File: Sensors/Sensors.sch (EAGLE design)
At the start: 32 parts, among them J2 JST_CONNECTOR, J6 JST_CONNECTOR, J7 JST_CONNECTOR, J8 JST_CONNECTOR, J9 JST_CONNECTOR

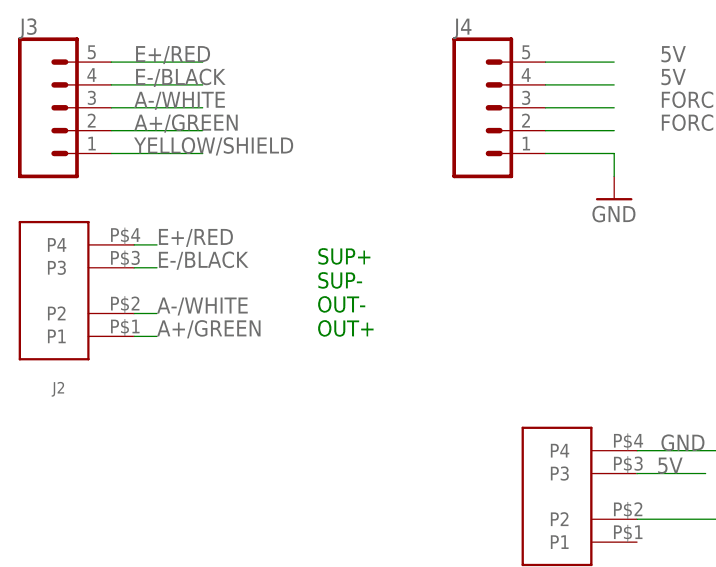
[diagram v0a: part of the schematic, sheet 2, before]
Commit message: Rewired force JST mount
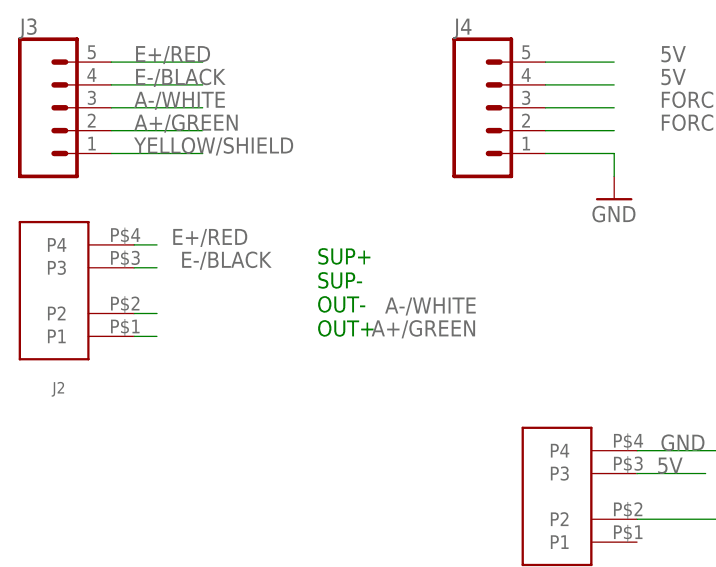
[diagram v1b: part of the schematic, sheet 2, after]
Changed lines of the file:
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@@
 <pinref part="J2" gate="G$1" pin="P4"/>
 <wire x1="2.54" y1="99.06" x2="5.08" y2="99.06" width="0.1524" layer="91"/>
-<label x="5.08" y="99.06" size="1.778" layer="95"/>
+<label x="15.24" y="99.06" size="1.778" layer="95" align="bottom-right"/>
 </segment>
 </net>
@@
 <pinref part="J2" gate="G$1" pin="P3"/>
 <wire x1="2.54" y1="96.52" x2="5.08" y2="96.52" width="0.1524" layer="91"/>
-<label x="5.08" y="96.52" size="1.778" layer="95"/>
+<label x="17.78" y="96.52" size="1.778" layer="95" align="bottom-right"/>
 </segment>
 </net>
@@
 <pinref part="J2" gate="G$1" pin="P2"/>
 <wire x1="2.54" y1="91.44" x2="5.08" y2="91.44" width="0.1524" layer="91"/>
-<label x="5.08" y="91.44" size="1.778" layer="95"/>
+<label x="40.64" y="91.44" size="1.778" layer="95" align="bottom-right"/>
 </segment>
 </net>
@@
 <pinref part="J2" gate="G$1" pin="P1"/>
 <wire x1="2.54" y1="88.9" x2="5.08" y2="88.9" width="0.1524" layer="91"/>
-<label x="5.08" y="88.9" size="1.778" layer="95"/>
+<label x="40.64" y="88.9" size="1.778" layer="95" align="bottom-right"/>
 </segment>
 </net>

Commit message: Refixed names on load cell JST
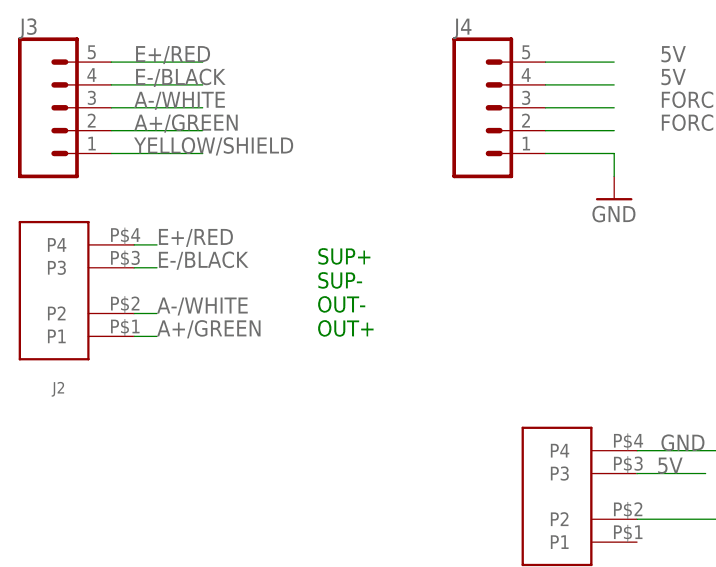
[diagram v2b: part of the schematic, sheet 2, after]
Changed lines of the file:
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@@
 <pinref part="J2" gate="G$1" pin="P4"/>
 <wire x1="2.54" y1="99.06" x2="5.08" y2="99.06" width="0.1524" layer="91"/>
-<label x="15.24" y="99.06" size="1.778" layer="95" align="bottom-right"/>
+<label x="5.08" y="99.06" size="1.778" layer="95"/>
 </segment>
 </net>
@@
 <pinref part="J2" gate="G$1" pin="P3"/>
 <wire x1="2.54" y1="96.52" x2="5.08" y2="96.52" width="0.1524" layer="91"/>
-<label x="17.78" y="96.52" size="1.778" layer="95" align="bottom-right"/>
+<label x="5.08" y="96.52" size="1.778" layer="95"/>
 </segment>
 </net>
@@
 <pinref part="J2" gate="G$1" pin="P2"/>
 <wire x1="2.54" y1="91.44" x2="5.08" y2="91.44" width="0.1524" layer="91"/>
-<label x="40.64" y="91.44" size="1.778" layer="95" align="bottom-right"/>
+<label x="5.08" y="91.44" size="1.778" layer="95"/>
 </segment>
 </net>
@@
 <pinref part="J2" gate="G$1" pin="P1"/>
 <wire x1="2.54" y1="88.9" x2="5.08" y2="88.9" width="0.1524" layer="91"/>
-<label x="40.64" y="88.9" size="1.778" layer="95" align="bottom-right"/>
+<label x="5.08" y="88.9" size="1.778" layer="95"/>
 </segment>
 </net>
